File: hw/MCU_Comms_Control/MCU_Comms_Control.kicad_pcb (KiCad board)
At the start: 4 copper layers, 46.7 x 68.8 mm, 56 parts, among them J1 USB_B_Mini, J2 CAN BUS, J3 TO_POWER_BOARD, J4 Mini-Debugging, J5 MULTI, J6 TEMP, SW1 BOOT, SW2 BUTTON, U1 SRV05-4, U2 SN65HVD230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

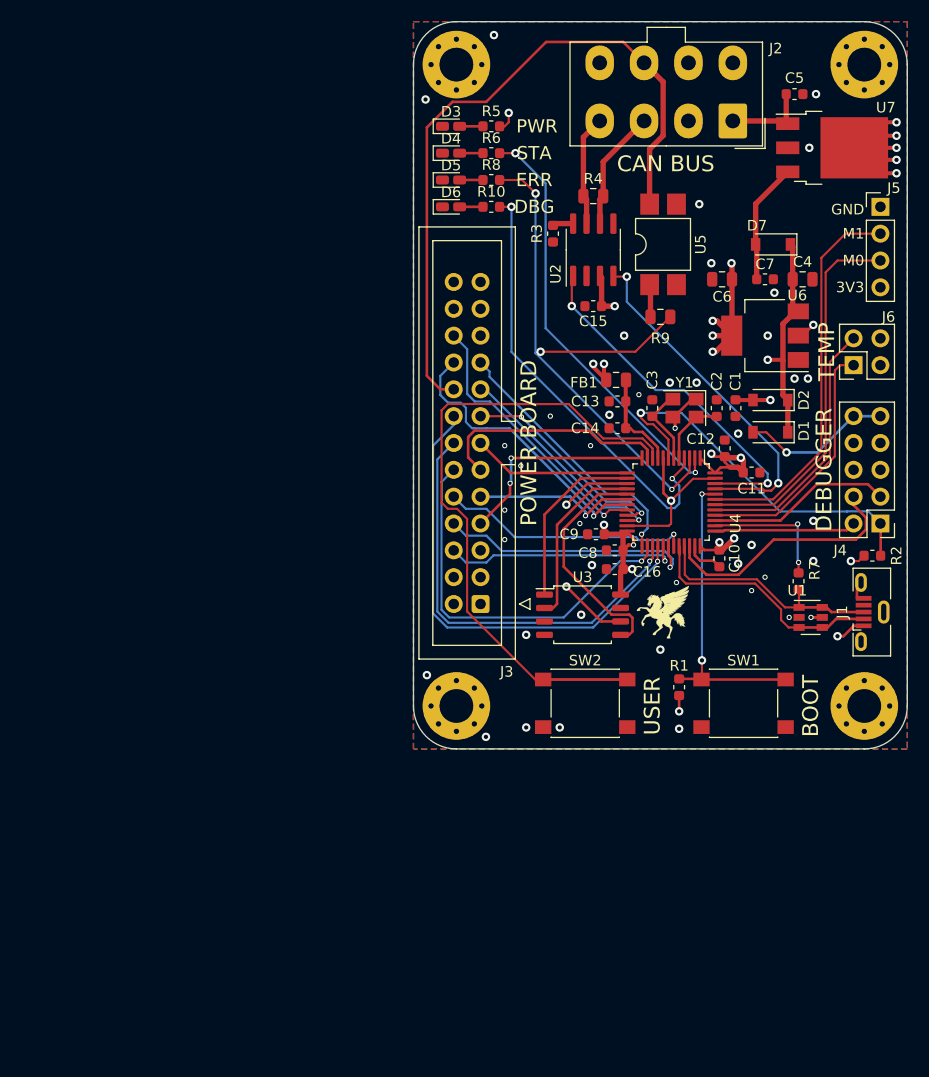
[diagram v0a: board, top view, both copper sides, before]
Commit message: add lqfp64 board version
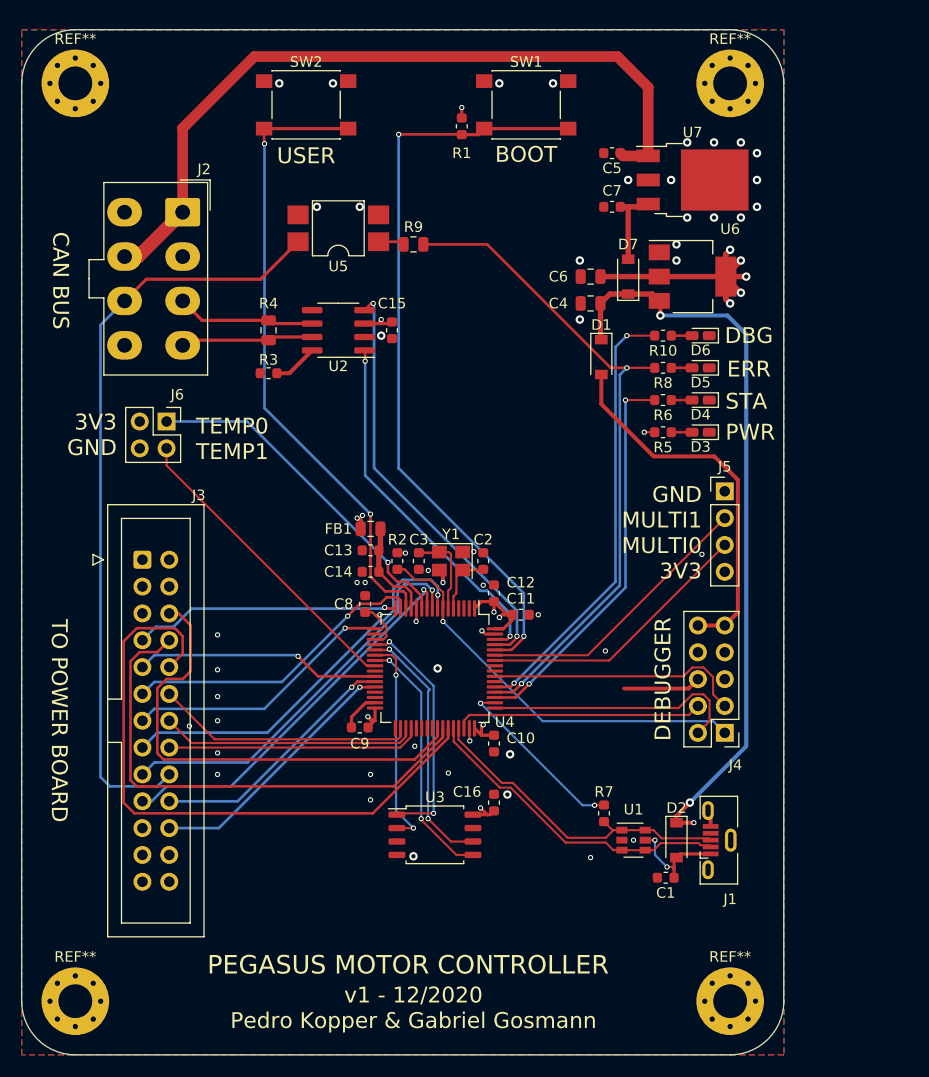
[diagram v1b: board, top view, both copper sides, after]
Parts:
- removed G***: LOGO, Custom:pegasus_large
- removed G***: LOGO, Custom:pegasus
- removed the REF** at (108.7, 45.5)
- removed the REF** at (70.1, 45.5)
- removed the REF** at (108.7, 106.2)
- removed the REF** at (70.1, 106.2)
- added REF**: MountingHole_3.2mm_M3_Pad_Via, MountingHole:MountingHole_3.2mm_M3_Pad_Via, F.Cu at (96.0, 47.2)
- added REF**: MountingHole_3.2mm_M3_Pad_Via, MountingHole:MountingHole_3.2mm_M3_Pad_Via, F.Cu at (96.0, 134.1)
- added REF**: MountingHole_3.2mm_M3_Pad_Via, MountingHole:MountingHole_3.2mm_M3_Pad_Via, F.Cu at (34.0, 134.1)
- added REF**: MountingHole_3.2mm_M3_Pad_Via, MountingHole:MountingHole_3.2mm_M3_Pad_Via, F.Cu at (34.0, 47.2)
- U4: value STM32F303CCTx -> STM32F303RCTx; footprint Package_QFP:LQFP-48_7x7mm_P0.5mm -> Package_QFP:LQFP-64_10x10mm_P0.5mm
- moved J6 65.2 mm to (42.7, 79.2), turned to 270 degrees
- moved SW2 62.5 mm to (55.9, 49.3), turned to 180 degrees
- moved SW1 60.3 mm to (76.7, 49.3), turned to 180 degrees
- moved R1 56.9 mm to (70.6, 51.3), turned to 90 degrees
- moved J2 52.8 mm to (44.2, 59.4), turned to 270 degrees
- moved R2 45.0 mm to (64.5, 92.5), turned to 90 degrees
- moved C1 44.9 mm to (89.9, 122.4), turned to 180 degrees
- moved D2 42.6 mm to (90.9, 118.9), turned to 270 degrees
- moved D3 37.4 mm to (93.2, 80.3), turned to 180 degrees
- moved R4 33.3 mm to (52.3, 70.6), turned to 90 degrees
- moved D4 33.2 mm to (93.2, 77.2), turned to 180 degrees
- moved R5 33.2 mm to (89.7, 80.3), turned to 180 degrees
- moved J3 32.3 mm to (40.4, 92.3), turned to 0 degrees
- moved U5 30.8 mm to (58.9, 61.0), turned to 180 degrees
- moved J5 30.7 mm to (95.5, 85.9)
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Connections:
- U4 pad 10: BUTTON -> HALL1
- U4 pad 11: CURR_V -> Net-(J6-Pad1)
- U4 pad 12: NTC_PWR -> GND
- U4 pad 13: CURR_W -> +3.3VADC
- U4 pad 14: ~FLASH_CS -> BUTTON
- U4 pad 15: FLASH_CLK -> CURR_V
- U4 pad 16: FLASH_MISO -> NTC_PWR
- U4 pad 17: FLASH_MOSI -> CURR_W
- U4 pad 18: CURR_U -> Net-(U4-Pad18)
- U4 pad 19: ENABLE -> +3V3
- U4 pad 2: STATUS -> Net-(U4-Pad2)
- U4 pad 20: VBUS_SCALED -> ~FLASH_CS
- U4 pad 21: HALL3 -> FLASH_CLK
- U4 pad 22: HALL2 -> FLASH_MISO
- U4 pad 23: GND -> FLASH_MOSI
- U4 pad 24: +3V3 -> Net-(J6-Pad2)
- U4 pad 25: HALL1 -> Net-(U4-Pad25)
- U4 pad 26: U_L -> CURR_U
- U4 pad 27: V_L -> ENABLE
- U4 pad 28: W_L -> VBUS_SCALED
- U4 pad 29: U_H -> Net-(U4-Pad29)
- U4 pad 3: ERR_OUT -> Net-(U4-Pad3)
- U4 pad 30: V_H -> Net-(U4-Pad30)
- U4 pad 31: W_H -> GND
- U4 pad 32: USB_D- -> +3V3
- U4 pad 33: USB_D+ -> Net-(U4-Pad33)
- U4 pad 34: SWDIO -> U_L
- U4 pad 35: GND -> V_L
- U4 pad 36: +3V3 -> W_L
- U4 pad 37: SWCLK -> Net-(U4-Pad37)
- U4 pad 38: Net-(R7-Pad2) -> Net-(U4-Pad38)
- U4 pad 39: SWO -> Net-(U4-Pad39)
- U4 pad 4: DEBUG_LED -> Net-(U4-Pad4)
- U4 pad 40: Net-(J6-Pad1) -> Net-(U4-Pad40)
- U4 pad 41: Net-(J6-Pad2) -> U_H
- U4 pad 42: MULTI0 -> V_H
- U4 pad 43: MULTI1 -> W_H
- U4 pad 44: ~BOOT -> USB_D-
- U4 pad 45: CAN_RX -> USB_D+
- U4 pad 46: CAN_TX -> SWDIO
- U4 pad 8: GND -> HALL3
- U4 pad 9: +3.3VADC -> HALL2
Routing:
- net +5V: track 49.0 -> 128.7 mm, vias 1 -> 3
- net +12V: track 86.4 -> 140.2 mm
- net ~BOOT: track 28.9 -> 72.1 mm
- net W_H: track 23.9 -> 60.1 mm, vias 1 -> 0
- net GND: track 47.6 -> 18.8 mm, vias 47 -> 51
- net Net-(C1-Pad1): track 33.9 -> 10.1 mm, vias 3 -> 2
- net V_H: track 25.3 -> 48.3 mm, vias 1 -> 0
- net U_H: track 22.7 -> 45.3 mm, vias 1 -> 0
- net W_L: track 45.4 -> 24.1 mm, vias 1 -> 0
- net Net-(D1-Pad2): track 14.3 -> 35.5 mm, vias 1 -> 0
- net HALL3: track 20.5 -> 38.1 mm, vias 2 -> 1
- net V_L: track 41.3 -> 24.3 mm, vias 1 -> 0
- net HALL2: track 21.2 -> 38.2 mm
- net U_L: track 36.8 -> 24.6 mm, vias 1 -> 0
- net HALL1: track 25.6 -> 37.0 mm
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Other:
- board size 46.7 x 68.8 mm -> 72.1 x 97 mm
- net class Default: clearance 0.2 -> 0.1524
- net class HIGHPWR added: clearance 0.5, trace_width 1.016, via_dia 0.8, via_drill 0.4
- net class LOWPWR added: clearance 0.2, trace_width 0.508, via_dia 0.8, via_drill 0.4
- net class VBUS added: clearance 0.5, trace_width 0.25, via_dia 0.8, via_drill 0.4
- rule trace_clearance: 0.2 -> 0.1524
- rule trace_min: 0.2 -> 0.1
- board text added: "3V3 GND"
- board text added: "GND MULTI1 MULTI0 3V3"
- board text added: "PEGASUS MOTOR CONTROLLER"
- board text added: "Stackup JLC2313"
- board text added: "TEMP0 TEMP1"
- board text added: "TO POWER BOARD"
- board text added: "v1 - 12/2020 Pedro Kopper & Gabriel Gosmann"
- board text removed: "3V3"
- board text removed: "GND"
- board text removed: "M0"
- board text removed: "M1"
- board text removed: "PEGASUS Motor Controller v1 11/2020 PEDRO KOPPER GABRIEL GOSMANN"
- board text removed: "POWER BOARD"
- board text removed: "TEMP"

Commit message: finish new control board revision
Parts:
- added D8: FAULT, LED_SMD:LED_0603_1608Metric_Castellated, F.Cu at (47.9, 94.9)
- added G***: LOGO, Custom:repo_qrcode, B.Cu at (67.1, 96.5)
- added G***: LOGO, Custom:pegasus_large, F.Cu at (67.7, 80.1)
- added J7: CAN, Connector_PinHeader_2.54mm:PinHeader_1x02_P2.54mm_Vertical, F.Cu at (49.7, 71.9)
- added JP1: USB PULL, Jumper:SolderJumper-2_P1.3mm_Open_RoundedPad1.0x1.5mm, F.Cu at (86.9, 115.3)
- added R11: 1k5, Resistor_SMD:R_0603_1608Metric, F.Cu at (47.9, 91.6)
- added REF**: KiCad-Logo2_8mm_SilkScreen, Symbol:KiCad-Logo2_8mm_SilkScreen, B.Cu at (65.9, 129.5)
- added REF**: ESD-Logo_6.6x6mm_SilkScreen, Symbol:ESD-Logo_6.6x6mm_SilkScreen, F.Cu at (87.4, 48.1)
- J5: footprint Connector_PinHeader_2.54mm:PinHeader_1x04_P2.54mm_Vertical -> Connector_PinHeader_2.54mm:PinHeader_1x06_P2.54mm_Vertical
- moved J5 11.2 mm to (95.4, 97.0), turned to 180 degrees
- moved J4 3.05 mm to (95.5, 111.8)
- moved R3 1.02 mm to (53.3, 74.7)
- moved R4 1.02 mm to (53.3, 70.6)
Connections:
- J5 pad 1: GND -> +3V3
- J5 pad 2: MULTI1 -> MULTI0
- J5 pad 3: MULTI0 -> MULTI1
- J5 pad 4: +3V3 -> MULTI2
- U4 pad 25: Net-(U4-Pad25) -> ERR_IN
- U4 pad 56: Net-(U4-Pad56) -> MULTI0
- U4 pad 57: Net-(U4-Pad57) -> MULTI1
- U4 pad 58: MULTI0 -> MULTI2
- U4 pad 59: MULTI1 -> MULTI3
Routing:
- net ~ERROR: track 72.1 -> 106.0 mm
- net MULTI3: track 0.00 -> 27.6 mm
- net MULTI2: track 0.00 -> 26.8 mm
- net ERR_IN: track 0.00 -> 19.9 mm
- net Net-(D1-Pad2): track 35.5 -> 40.6 mm
- net +3V3: track 55.9 -> 58.4 mm, vias 17 -> 19
- net ~RESET: track 39.0 -> 41.2 mm
- net GND: track 18.8 -> 16.7 mm, vias 51 -> 52
- net USB_D+: track 30.7 -> 32.7 mm
- net +5V: track 128.7 -> 129.9 mm
- net MULTI0: track 26.3 -> 25.1 mm
- net MULTI1: track 27.1 -> 26.1 mm
- net Net-(R3-Pad1): track 4.24 -> 3.22 mm
- net SWO: track 24.6 -> 25.3 mm
- net CAN_H: track 12.6 -> 13.3 mm
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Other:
- board text added: "FAULT!"
- board text added: "GND MULTI3 MULTI2 MULTI1 MULTI0 3V3"
- board text added: "H"
- board text added: "L"
- board text added: "https://github.com/phckopper/projeto-inversor-pmsm"
- board text added: "pedrohkopper@gmail.com gabriel.gosmann@gmail.com"
- board text removed: "GND MULTI1 MULTI0 3V3"

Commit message: specify order number location on pcb
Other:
- board text added: "JLCJLCJLCJLC"
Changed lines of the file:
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@@
   (general
     (thickness 1.6)
-    (drawings 28)
+    (drawings 29)
     (tracks 600)
     (zones 0)
@@
     )
   )
+  (gr_text JLCJLCJLCJLC (at 76.708 49.276) (layer F.SilkS)
+    (effects (font (size 1 0.8) (thickness 0.1)))
+  )
   (gr_text https://github.com/phckopper/projeto-inversor-pmsm (at 65.532 54.356) (layer B.SilkS)
